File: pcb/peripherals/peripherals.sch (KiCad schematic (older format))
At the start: 11 parts, among them Q1 RQ3E100BNTB, U1 DGD0506A

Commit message: Save before autofill
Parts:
- removed C1: 10uF, symbol Device:C_Small
- removed C2: 470uF, Capacitors_ThroughHole:CP_Radial_D10.0mm_P5.00mm, symbol Device:C_Small
- removed C3: 1000uF, Capacitors_ThroughHole:CP_Radial_D18.0mm_P7.50mm, symbol Device:C_Small
- removed C4: 100nF, symbol Device:C_Small
- removed L1: 100uH, symbol Device:L_Small
- removed Q1, Q?: RQ3E100BNTB, peripherals:Rohm-HSMT8, symbol peripherals:Q_NMOS_SSSGDDDD
- removed R1, R3: 0, symbol Device:R_Small
- removed R2: 10k, symbol Device:R_Small
- removed U1: DGD0506A, symbol peripherals:DGD0506A
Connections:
- net labels removed: +BATT, GND
- wire segments 62 -> 0

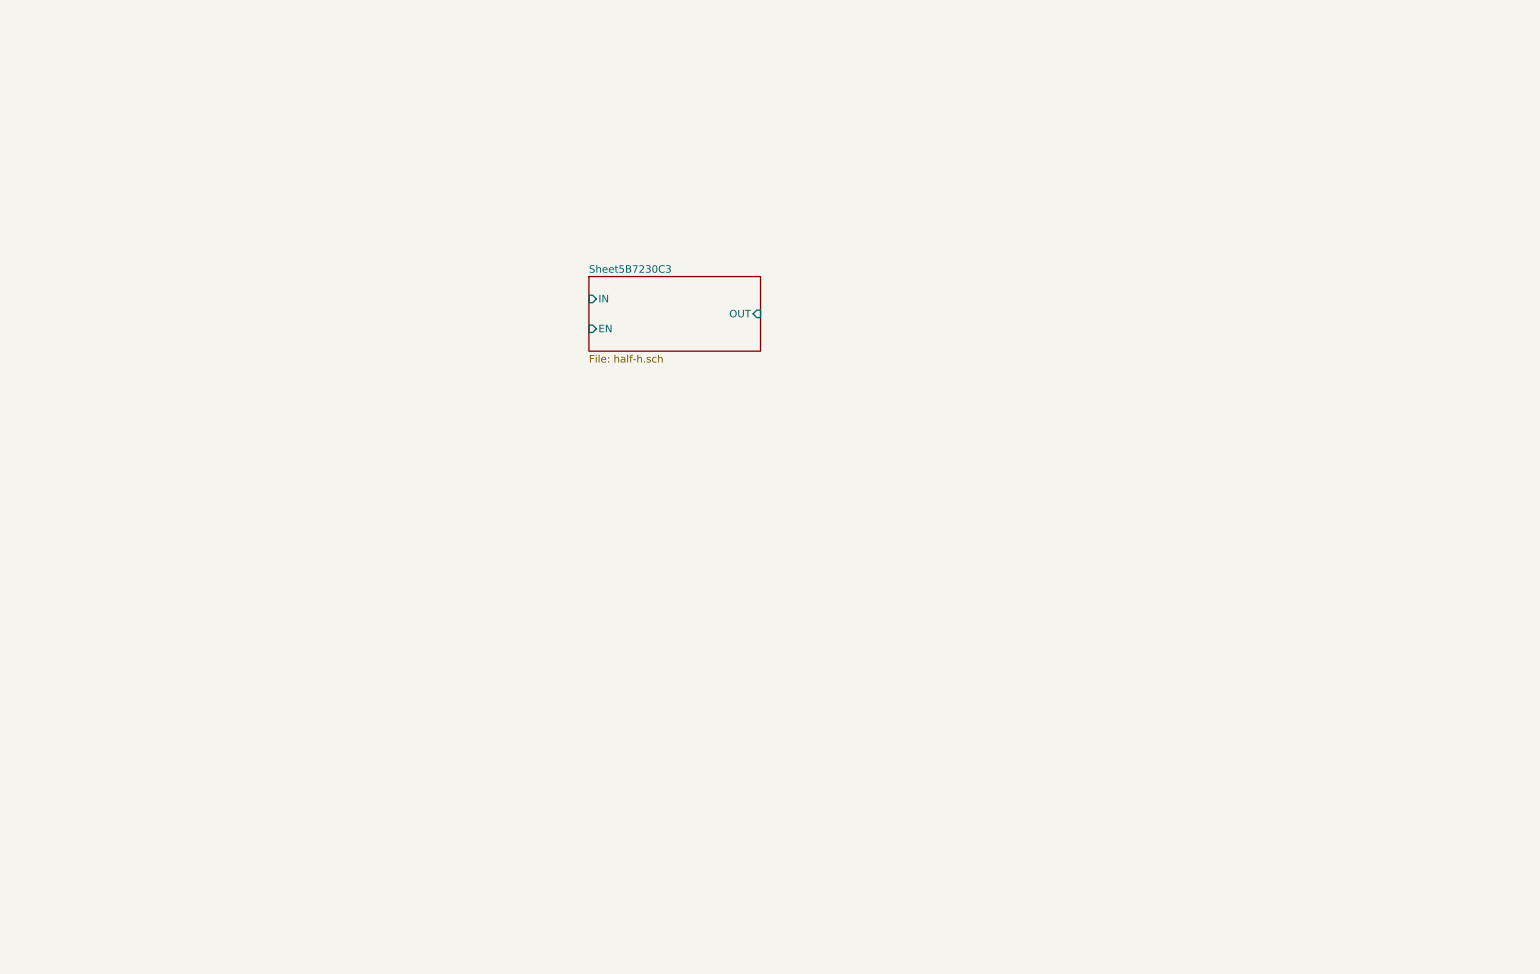
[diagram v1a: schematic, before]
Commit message: Schematic done; TODO add footprints for connectors
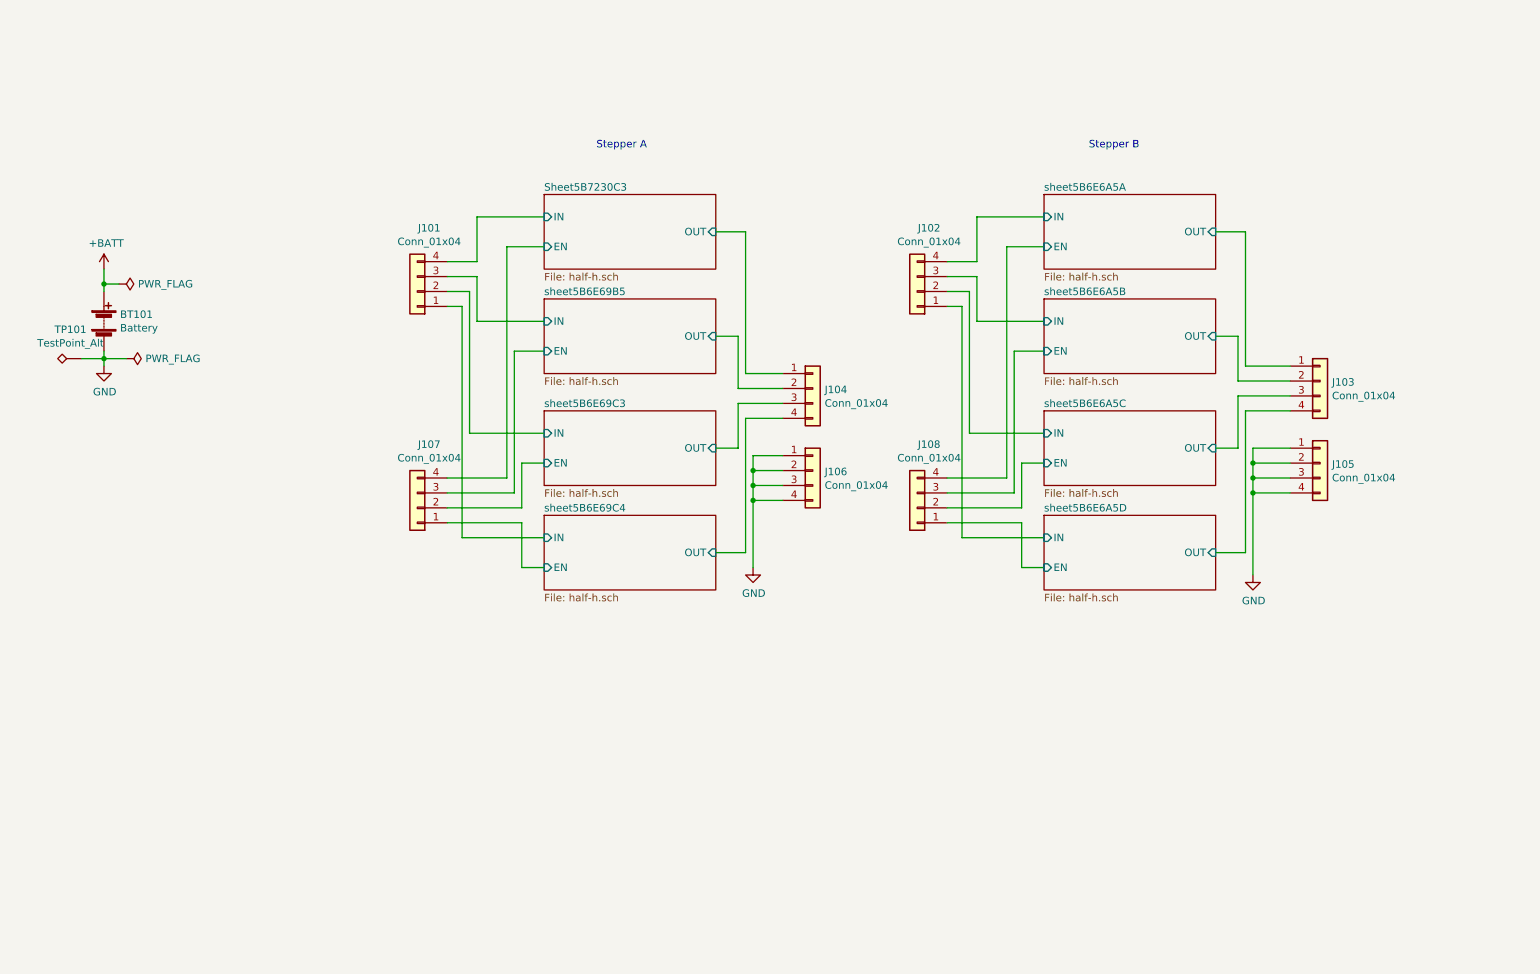
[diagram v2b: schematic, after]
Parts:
- added BT101: Battery, symbol Device:Battery
- added J101, J102, J103, J104, J105, J106, J107, J108: Conn_01x04, symbol Connector_Generic:Conn_01x04
- added TP101: TestPoint_Alt, symbol Connector:TestPoint_Alt
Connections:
- net Sheet5B7230C3/EN: now also J107.4 (Pin_4)
- net Sheet5B7230C3/IN: now also J101.4 (Pin_4)
- net Sheet5B7230C3/OUT: now also J104.1 (Pin_1)
- new net +BATT: BT101.1 (+)
- new net GND: BT101.2 (-), J105.1 (Pin_1), J105.2 (Pin_2), J105.3 (Pin_3), J105.4 (Pin_4), J106.1 (Pin_1), J106.2 (Pin_2), J106.3 (Pin_3), J106.4 (Pin_4), TP101.1
- new net sheet5B6E69B5/EN: J107.3 (Pin_3)
- new net sheet5B6E69B5/IN: J101.3 (Pin_3)
- new net sheet5B6E69B5/OUT: J104.2 (Pin_2)
- new net sheet5B6E69C3/EN: J107.2 (Pin_2)
- new net sheet5B6E69C3/IN: J101.2 (Pin_2)
- new net sheet5B6E69C3/OUT: J104.3 (Pin_3)
- new net sheet5B6E69C4/EN: J107.1 (Pin_1)
- new net sheet5B6E69C4/IN: J101.1 (Pin_1)
- new net sheet5B6E69C4/OUT: J104.4 (Pin_4)
- new net sheet5B6E6A5A/EN: J108.4 (Pin_4)
- new net sheet5B6E6A5A/IN: J102.4 (Pin_4)
- new net sheet5B6E6A5A/OUT: J103.1 (Pin_1)
- new net sheet5B6E6A5B/EN: J108.3 (Pin_3)
- new net sheet5B6E6A5B/IN: J102.3 (Pin_3)
- new net sheet5B6E6A5B/OUT: J103.2 (Pin_2)
- new net sheet5B6E6A5C/EN: J108.2 (Pin_2)
- new net sheet5B6E6A5C/IN: J102.2 (Pin_2)
- new net sheet5B6E6A5C/OUT: J103.3 (Pin_3)
- new net sheet5B6E6A5D/EN: J108.1 (Pin_1)
- new net sheet5B6E6A5D/IN: J102.1 (Pin_1)
- new net sheet5B6E6A5D/OUT: J103.4 (Pin_4)
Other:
- note added: "Stepper A"
- note added: "Stepper B"

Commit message: Save before autofill
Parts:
- BT101: footprint (none) -> peripherals:Conn-2-8mmx6mm; Mouser (none) -> NoPart
- J101, J102, J103, J104, J105, J106, J107, J108: footprint (none) -> peripherals:Conn-4-8mmx6mm; Mouser (none) -> NoPart
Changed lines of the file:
@@
 F 0 "J104" H 5930 3042 50  0000 L CNN
 F 1 "Conn_01x04" H 5930 2951 50  0000 L CNN
-F 2 "" H 5850 3050 50  0001 C CNN
+F 2 "peripherals:Conn-4-8mmx6mm" H 5850 3050 50  0001 C CNN
 F 3 "~" H 5850 3050 50  0001 C CNN
+F 4 "NoPart" H 5850 3050 50  0001 C CNN "Mouser"
 	1    5850 3050
 	1    0    0    -1
@@
 F 0 "J103" H 9330 2992 50  0000 L CNN
 F 1 "Conn_01x04" H 9330 2901 50  0000 L CNN
-F 2 "" H 9250 3000 50  0001 C CNN
+F 2 "peripherals:Conn-4-8mmx6mm" H 9250 3000 50  0001 C CNN
 F 3 "~" H 9250 3000 50  0001 C CNN
+F 4 "NoPart" H 9250 3000 50  0001 C CNN "Mouser"
 	1    9250 3000
 	1    0    0    -1
@@
 F 0 "J106" H 5930 3592 50  0000 L CNN
 F 1 "Conn_01x04" H 5930 3501 50  0000 L CNN
-F 2 "" H 5850 3600 50  0001 C CNN
+F 2 "peripherals:Conn-4-8mmx6mm" H 5850 3600 50  0001 C CNN
 F 3 "~" H 5850 3600 50  0001 C CNN
+F 4 "NoPart" H 5850 3600 50  0001 C CNN "Mouser"
 	1    5850 3600
 	1    0    0    -1
@@
 F 0 "J105" H 9330 3542 50  0000 L CNN
 F 1 "Conn_01x04" H 9330 3451 50  0000 L CNN
-F 2 "" H 9250 3550 50  0001 C CNN
+F 2 "peripherals:Conn-4-8mmx6mm" H 9250 3550 50  0001 C CNN
 F 3 "~" H 9250 3550 50  0001 C CNN
+F 4 "NoPart" H 9250 3550 50  0001 C CNN "Mouser"
 	1    9250 3550
 	1    0    0    -1
@@
 F 0 "BT101" H 1208 2646 50  0000 L CNN
 F 1 "Battery" H 1208 2555 50  0000 L CNN
-F 2 "" V 1100 2660 50  0001 C CNN
+F 2 "peripherals:Conn-2-8mmx6mm" V 1100 2660 50  0001 C CNN
 F 3 "~" V 1100 2660 50  0001 C CNN
+F 4 "NoPart" H 1100 2600 50  0001 C CNN "Mouser"
 	1    1100 2600
 	1    0    0    -1
@@
 F 0 "J101" H 3120 1975 50  0000 C CNN
 F 1 "Conn_01x04" H 3120 2066 50  0000 C CNN
-F 2 "" H 3200 2400 50  0001 C CNN
+F 2 "peripherals:Conn-4-8mmx6mm" H 3200 2400 50  0001 C CNN
 F 3 "~" H 3200 2400 50  0001 C CNN
+F 4 "NoPart" H 3200 2400 50  0001 C CNN "Mouser"
 	1    3200 2400
 	-1   0    0    1
@@
 F 0 "J107" H 3120 3425 50  0000 C CNN
 F 1 "Conn_01x04" H 3120 3516 50  0000 C CNN
-F 2 "" H 3200 3850 50  0001 C CNN
+F 2 "peripherals:Conn-4-8mmx6mm" H 3200 3850 50  0001 C CNN
 F 3 "~" H 3200 3850 50  0001 C CNN
+F 4 "NoPart" H 3200 3850 50  0001 C CNN "Mouser"
 	1    3200 3850
 	-1   0    0    1
@@
 F 0 "J102" H 6470 1975 50  0000 C CNN
 F 1 "Conn_01x04" H 6470 2066 50  0000 C CNN
-F 2 "" H 6550 2400 50  0001 C CNN
+F 2 "peripherals:Conn-4-8mmx6mm" H 6550 2400 50  0001 C CNN
 F 3 "~" H 6550 2400 50  0001 C CNN
+F 4 "NoPart" H 6550 2400 50  0001 C CNN "Mouser"
 	1    6550 2400
 	-1   0    0    1
@@
 F 0 "J108" H 6470 3425 50  0000 C CNN
 F 1 "Conn_01x04" H 6470 3516 50  0000 C CNN
-F 2 "" H 6550 3850 50  0001 C CNN
+F 2 "peripherals:Conn-4-8mmx6mm" H 6550 3850 50  0001 C CNN
 F 3 "~" H 6550 3850 50  0001 C CNN
+F 4 "NoPart" H 6550 3850 50  0001 C CNN "Mouser"
 	1    6550 3850
 	-1   0    0    1

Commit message: Save before messing with tiler script
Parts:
- J101, J102, J107, J108: footprint peripherals:Conn-4-8mmx6mm -> Socket_Strips:Socket_Strip_Straight_1x04_Pitch2.54mm
- TP101: footprint (none) -> Measurement_Points:Measurement_Point_Round-SMD-Pad_Small; Mouser (none) -> NoPart
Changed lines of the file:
@@
 F 0 "TP101" V 1145 2924 50  0000 C CNN
 F 1 "TestPoint_Alt" V 1054 2924 50  0000 C CNN
-F 2 "" H 1150 2850 50  0001 C CNN
+F 2 "Measurement_Points:Measurement_Point_Round-SMD-Pad_Small" H 1150 2850 50  0001 C CNN
 F 3 "~" H 1150 2850 50  0001 C CNN
+F 4 "NoPart" H 1150 2850 50  0001 C CNN "Mouser"
 	1    950  2850
 	0    -1   -1   0
@@
 F 0 "J101" H 3120 1975 50  0000 C CNN
 F 1 "Conn_01x04" H 3120 2066 50  0000 C CNN
-F 2 "peripherals:Conn-4-8mmx6mm" H 3200 2400 50  0001 C CNN
+F 2 "Socket_Strips:Socket_Strip_Straight_1x04_Pitch2.54mm" H 3200 2400 50  0001 C CNN
 F 3 "~" H 3200 2400 50  0001 C CNN
 F 4 "NoPart" H 3200 2400 50  0001 C CNN "Mouser"
@@
 F 0 "J107" H 3120 3425 50  0000 C CNN
 F 1 "Conn_01x04" H 3120 3516 50  0000 C CNN
-F 2 "peripherals:Conn-4-8mmx6mm" H 3200 3850 50  0001 C CNN
+F 2 "Socket_Strips:Socket_Strip_Straight_1x04_Pitch2.54mm" H 3200 3850 50  0001 C CNN
 F 3 "~" H 3200 3850 50  0001 C CNN
 F 4 "NoPart" H 3200 3850 50  0001 C CNN "Mouser"
@@
 F 0 "J102" H 6470 1975 50  0000 C CNN
 F 1 "Conn_01x04" H 6470 2066 50  0000 C CNN
-F 2 "peripherals:Conn-4-8mmx6mm" H 6550 2400 50  0001 C CNN
+F 2 "Socket_Strips:Socket_Strip_Straight_1x04_Pitch2.54mm" H 6550 2400 50  0001 C CNN
 F 3 "~" H 6550 2400 50  0001 C CNN
 F 4 "NoPart" H 6550 2400 50  0001 C CNN "Mouser"
@@
 F 0 "J108" H 6470 3425 50  0000 C CNN
 F 1 "Conn_01x04" H 6470 3516 50  0000 C CNN
-F 2 "peripherals:Conn-4-8mmx6mm" H 6550 3850 50  0001 C CNN
+F 2 "Socket_Strips:Socket_Strip_Straight_1x04_Pitch2.54mm" H 6550 3850 50  0001 C CNN
 F 3 "~" H 6550 3850 50  0001 C CNN
 F 4 "NoPart" H 6550 3850 50  0001 C CNN "Mouser"
